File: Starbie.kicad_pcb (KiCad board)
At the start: 2 copper layers, 122.8 x 66 mm, 7 parts, among them J1 Conn_01x08_Pin, J2 Conn_01x04_Pin, SW1 SW_Push, SW2 SW_Push, U1 DHT11, U2 XIAO-ESP32-C3-SMD

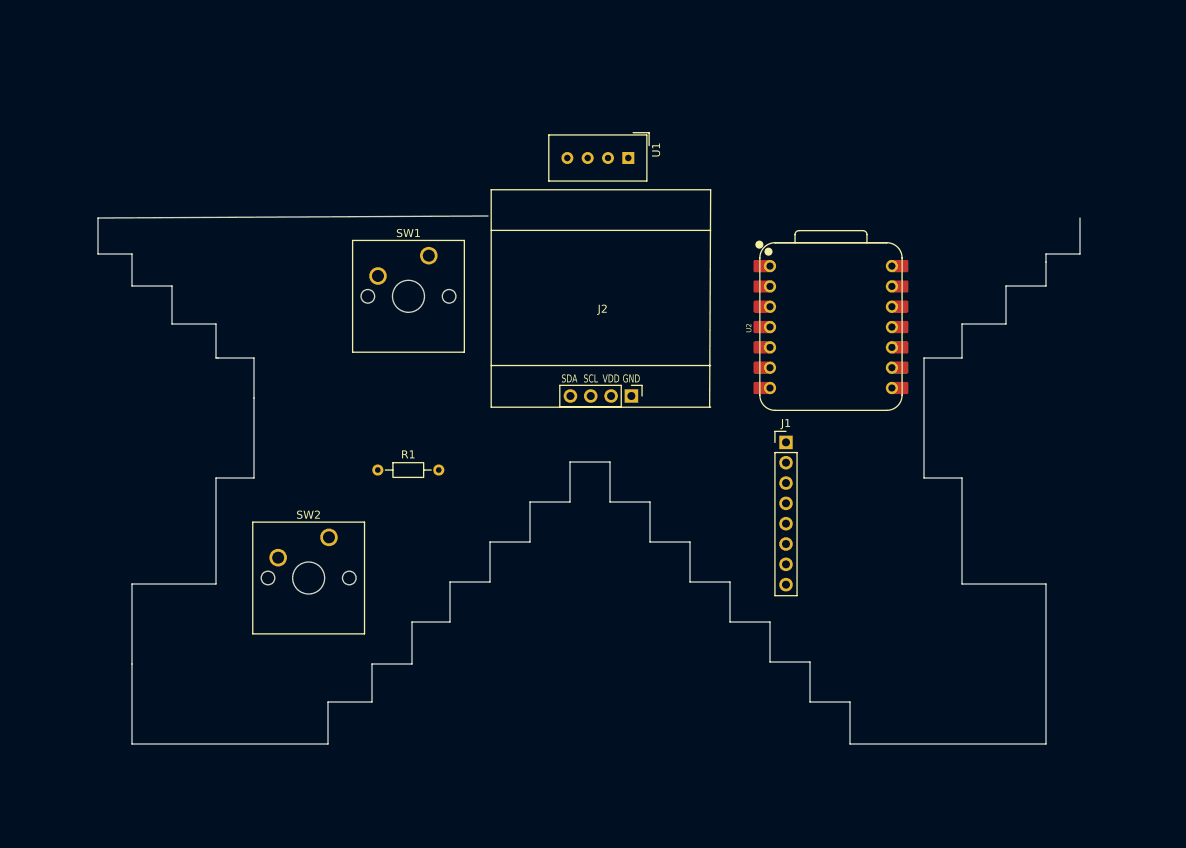
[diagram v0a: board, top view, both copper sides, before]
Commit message: Route PCB and add firmware sketch
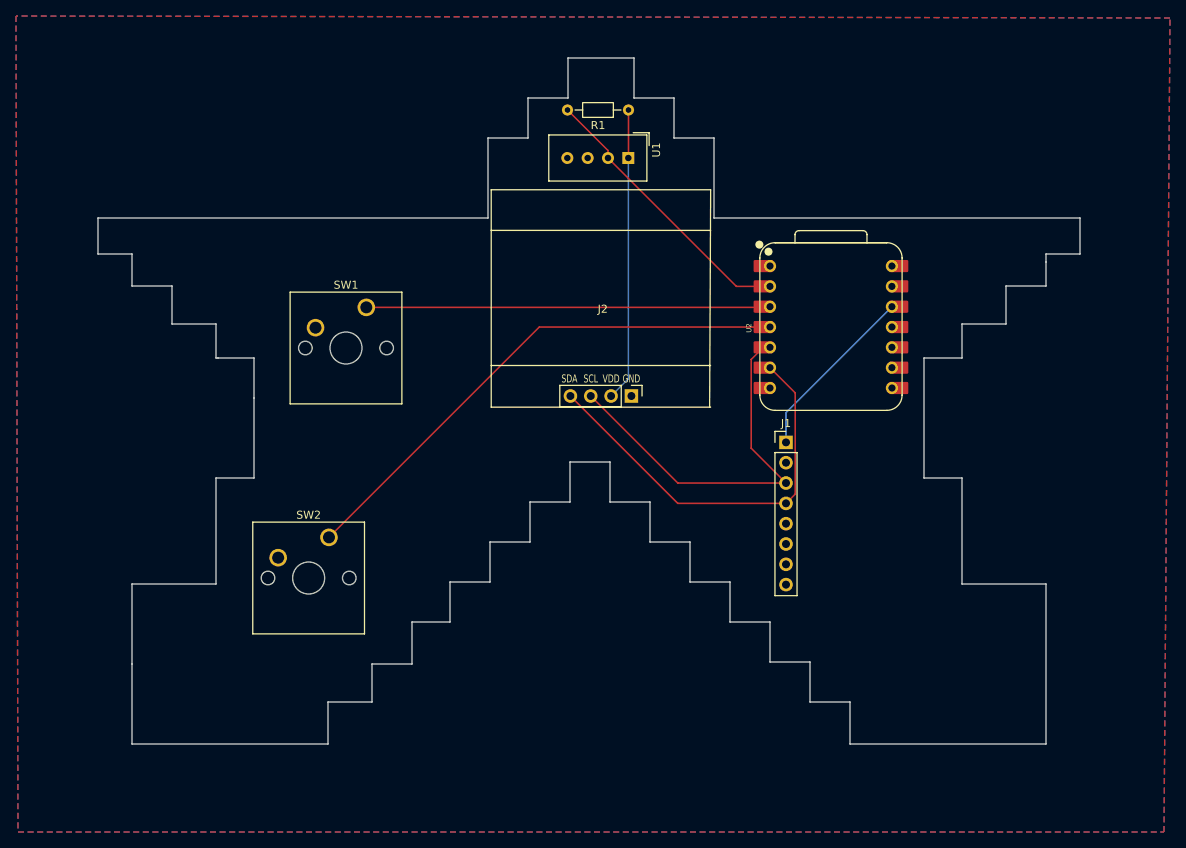
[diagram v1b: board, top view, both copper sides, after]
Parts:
- moved R1 54.8 mm to (159.8, 61.2), turned to 180 degrees
- moved SW1 10.1 mm to (127.0, 85.9)
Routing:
- net /GPIO3: track 0.00 -> 65.2 mm
- net +3.3V: track 0.00 -> 59.1 mm
- net /SDA: track 0.00 -> 51.2 mm
- net /GPIO2: track 0.00 -> 49.7 mm
- net /SCL: track 0.00 -> 49.1 mm
- net /DHT11 DATA: track 0.00 -> 34.2 mm
- added copper zone on B.Cu, net GND
- added copper zone on F.Cu, net GND
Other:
- board size 122.8 x 66 mm -> 122.8 x 85.8 mm

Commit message: Add gerbers, drill files and BOM csv format
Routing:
- net +3.3V: track 59.1 -> 83.4 mm
- net /SDA: track 51.2 -> 58.8 mm
- net /SCL: track 49.1 -> 53.1 mm
- net GND: vias 0 -> 2
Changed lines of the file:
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@@
 			(plot_on_all_layers_selection 0x00000000_00000000_00000000_00000000)
 			(disableapertmacros no)
-			(usegerberextensions no)
-			(usegerberattributes yes)
+			(usegerberextensions yes)
+			(usegerberattributes no)
 			(usegerberadvancedattributes yes)
 			(creategerberjobfile yes)
@@
 			(sketchdnponfab yes)
 			(crossoutdnponfab yes)
-			(subtractmaskfromsilk no)
+			(subtractmaskfromsilk yes)
 			(outputformat 1)
 			(mirror no)
-			(drillshape 1)
+			(drillshape 0)
 			(scaleselection 1)
-			(outputdirectory "")
+			(outputdirectory "production/gerbers/")
 		)
 	)
@@
 		(sheetname "/")
 		(sheetfile "Starbie.kicad_sch")
-		(units
-			(unit
-				(name "A")
-				(pins "1" "2" "3" "4")
-			)
-		)
 		(attr through_hole)
 		(duplicate_pad_numbers_are_jumpers no)
@@
 		(sheetname "/")
 		(sheetfile "Starbie.kicad_sch")
-		(units
-			(unit
-				(name "A")
-				(pins "1" "2" "3" "4" "5" "6" "7" "15" "16" "17" "21" "18" "22" "19"
-					"20" "14" "13" "12" "11" "10" "9" "8"
-				)
-			)
-		)
-		(attr smd)
+		(attr through_hole)
 		(duplicate_pad_numbers_are_jumpers no)
 		(fp_line
@@
 		(layer "Edge.Cuts")
 	)
+	(gr_line
+		(start 150.776 95.073)
+		(end 150.776 95.2)
+		(stroke
+			(width 0.05)
+			(type default)
+		)
+		(layer "F.CrtYd")
+	)
+	(gr_line
+		(start 161.976 95.073)
+		(end 161.976 95.2)
+		(stroke
+			(width 0.05)
+			(type default)
+		)
+		(layer "F.CrtYd")
+	)
 	(segment
 		(start 122.37 114.67)
@@
 		(net "GND")
 	)
+	(via
+		(at 166.5 68.25)
+		(size 0.6)
+		(drill 0.3)
+		(layers "F.Cu" "B.Cu")
+		(free yes)
+		(net "GND")
+	)
+	(via
+		(at 156.25 57.25)
+		(size 0.6)
+		(drill 0.3)
+		(layers "F.Cu" "B.Cu")
+		(free yes)
+		(net "GND")
+	)
 	(segment
 		(start 176.585 85.92)
@@
 	)
 	(segment
+		(start 163.436 102.8)
+		(end 179.5 102.8)
+		(width 0.2)
+		(layer "B.Cu")
+		(net "+3.3V")
+	)
+	(segment
 		(start 159.79 94.846)
 		(end 157.636 97)
@@
 	)
 	(segment
+		(start 157.636 97)
+		(end 163.436 102.8)
+		(width 0.2)
+		(layer "B.Cu")
+		(net "+3.3V")
+	)
+	(segment
 		(start 179.5 102.8)
 		(end 179.5 99.08)
@@
 	)
 	(segment
-		(start 175.149 103.529)
-		(end 175.149 92.436)
+		(start 180.65 101.65)
+		(end 179.997786 101.65)
+		(width 0.2)
+		(layer "F.Cu")
+		(net "/SCL")
+	)
+	(segment
+		(start 182.25 105.75)
+		(end 182.25 103.25)
+		(width 0.2)
+		(layer "F.Cu")
+		(net "/SCL")
+	)
+	(segment
+		(start 175.149 96.801214)
+		(end 175.149 92.19337)
 		(width 0.2)
 		(layer "F.Cu")
@@
 	(segment
 		(start 179.5 107.88)
-		(end 175.149 103.529)
+		(end 180.12 107.88)
+		(width 0.2)
+		(layer "F.Cu")
+		(net "/SCL")
+	)
+	(segment
+		(start 175.149 92.19337)
+		(end 176.42237 90.92)
 		(width 0.2)
 		(layer "F.Cu")
@@
 	)
 	(segment
-		(start 175.149 92.436)
-		(end 176.665 90.92)
+		(start 176.42237 90.92)
+		(end 177.5 90.92)
 		(width 0.2)
 		(layer "F.Cu")
@@
 	)
 	(segment
-		(start 180.65 109.27)
-		(end 180.65 96.61)
+		(start 179.997786 101.65)
+		(end 175.149 96.801214)
 		(width 0.2)
 		(layer "F.Cu")
-		(net "/SDA")
+		(net "/SCL")
 	)
 	(segment
-		(start 179.5 110.42)
-		(end 180.65 109.27)
+		(start 180.12 107.88)
+		(end 182.25 105.75)
 		(width 0.2)
 		(layer "F.Cu")
-		(net "/SDA")
+		(net "/SCL")
+	)
+	(segment
+		(start 182.25 103.25)
+		(end 180.65 101.65)
+		(width 0.2)
+		(layer "F.Cu")
+		(net "/SCL")
 	)
 	(segment
@@
 	)
 	(segment
+		(start 183.5 110)
+		(end 183.5 94.25)
+		(width 0.2)
+		(layer "F.Cu")
+		(net "/SDA")
+	)
+	(segment
 		(start 152.556 97)
 		(end 165.976 110.42)
@@
 	)
 	(segment
-		(start 180.65 96.61)
+		(start 179.5 110.42)
+		(end 183.08 110.42)
+		(width 0.2)
+		(layer "F.Cu")
+		(net "/SDA")
+	)
+	(segment
+		(start 183.5 94.25)
+		(end 182.71 93.46)
+		(width 0.2)
+		(layer "F.Cu")
+		(net "/SDA")
+	)
+	(segment
+		(start 182.71 93.46)
 		(end 177.5 93.46)
 		(width 0.2)
 		(layer "F.Cu")
+		(net "/SDA")
+	)
+	(segment
+		(start 183.08 110.42)
+		(end 183.5 110)
+		(width 0.2)
+		(layer "F.Cu")
